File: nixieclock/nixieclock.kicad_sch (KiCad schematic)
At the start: 0 parts

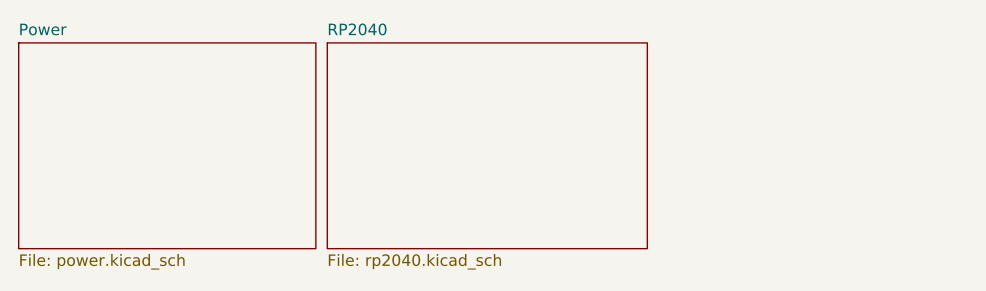
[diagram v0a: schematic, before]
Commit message: Start working on nixie tube stuff
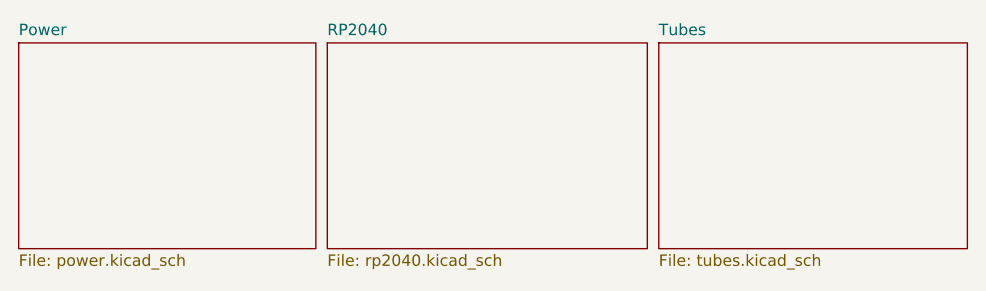
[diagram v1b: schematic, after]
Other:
- added sheet Tubes (tubes.kicad_sch)
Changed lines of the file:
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@@
+	)
+	(sheet
+		(at 83.82 12.7)
+		(size 34.29 22.86)
+		(exclude_from_sim no)
+		(in_bom yes)
+		(on_board yes)
+		(dnp no)
+		(fields_autoplaced yes)
+		(stroke
+			(width 0.1524)
+			(type solid)
+		)
+		(fill
+			(color 0 0 0 0.0000)
+		)
+		(property "Sheetname" "Tubes"
+			(at 83.82 11.9884 0)
+			(effects
+				(font
+					(size 1.27 1.27)
+				)
+				(justify left bottom)
+			)
+		)
+		(property "Sheetfile" "tubes.kicad_sch"
+			(at 83.82 36.1446 0)
+			(effects
+				(font
+					(size 1.27 1.27)
+				)
+				(justify left top)
+			)
+		)
+		(instances
+			(project "nixieclock"
+				(path "/36f98e0b-03c8-47d1-9b6f-a29babd2cb0f"
+					(page "4")
+				)
+			)
+		)
 	)
 	(sheet
